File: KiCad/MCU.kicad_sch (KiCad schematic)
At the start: 17 parts, among them U1 RaspberryPi_Pico

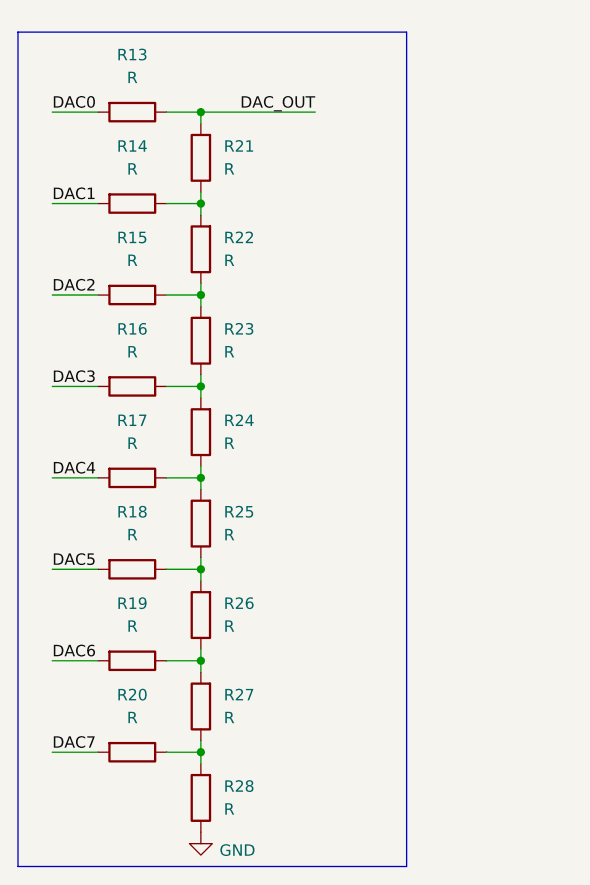
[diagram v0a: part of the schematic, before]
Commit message: Added elements values
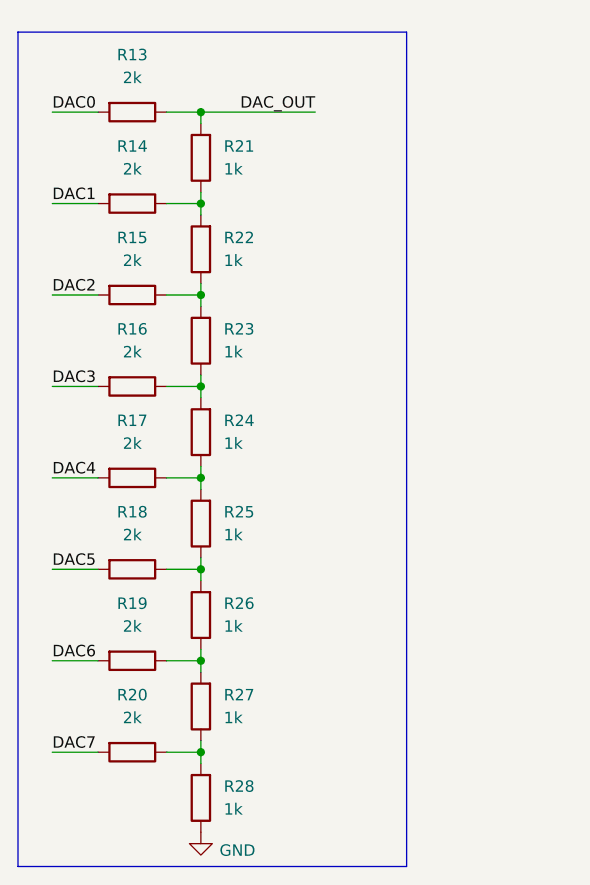
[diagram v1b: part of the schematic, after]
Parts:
- R13, R14, R15, R16, R17, R18, R19, R20: value R -> 2k
- R21, R22, R23, R24, R25, R26, R27, R28: value R -> 1k
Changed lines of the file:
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@@
 			)
 		)
-		(property "Value" "R"
+		(property "Value" "2k"
 			(at 78.74 132.08 90)
 			(effects
@@
 			)
 		)
-		(property "Value" "R"
+		(property "Value" "2k"
 			(at 78.74 71.12 90)
 			(effects
@@
 			)
 		)
-		(property "Value" "R"
+		(property "Value" "1k"
 			(at 88.9 111.7599 0)
 			(effects
@@
 			)
 		)
-		(property "Value" "R"
+		(property "Value" "2k"
 			(at 78.74 81.28 90)
 			(effects
@@
 			)
 		)
-		(property "Value" "R"
+		(property "Value" "2k"
 			(at 78.74 91.44 90)
 			(effects
@@
 			)
 		)
-		(property "Value" "R"
+		(property "Value" "1k"
 			(at 88.9 132.0799 0)
 			(effects
@@
 			)
 		)
-		(property "Value" "R"
+		(property "Value" "2k"
 			(at 78.74 121.92 90)
 			(effects
@@
 			)
 		)
-		(property "Value" "R"
+		(property "Value" "2k"
 			(at 78.74 60.96 90)
 			(effects
@@
 			)
 		)
-		(property "Value" "R"
+		(property "Value" "2k"
 			(at 78.74 111.76 90)
 			(effects
@@
 			)
 		)
-		(property "Value" "R"
+		(property "Value" "2k"
 			(at 78.74 101.6 90)
 			(effects
@@
 			)
 		)
-		(property "Value" "R"
+		(property "Value" "1k"
 			(at 88.9 71.1199 0)
 			(effects
@@
 			)
 		)
-		(property "Value" "R"
+		(property "Value" "1k"
 			(at 88.9 91.4399 0)
 			(effects
@@
 			)
 		)
-		(property "Value" "R"
+		(property "Value" "1k"
 			(at 88.9 101.5999 0)
 			(effects
@@
 			)
 		)
-		(property "Value" "R"
+		(property "Value" "1k"
 			(at 88.9 142.2399 0)
 			(effects
@@
 			)
 		)
-		(property "Value" "R"
+		(property "Value" "1k"
 			(at 88.9 121.9199 0)
 			(effects
@@
 			)
 		)
-		(property "Value" "R"
+		(property "Value" "1k"
 			(at 88.9 81.2799 0)
 			(effects

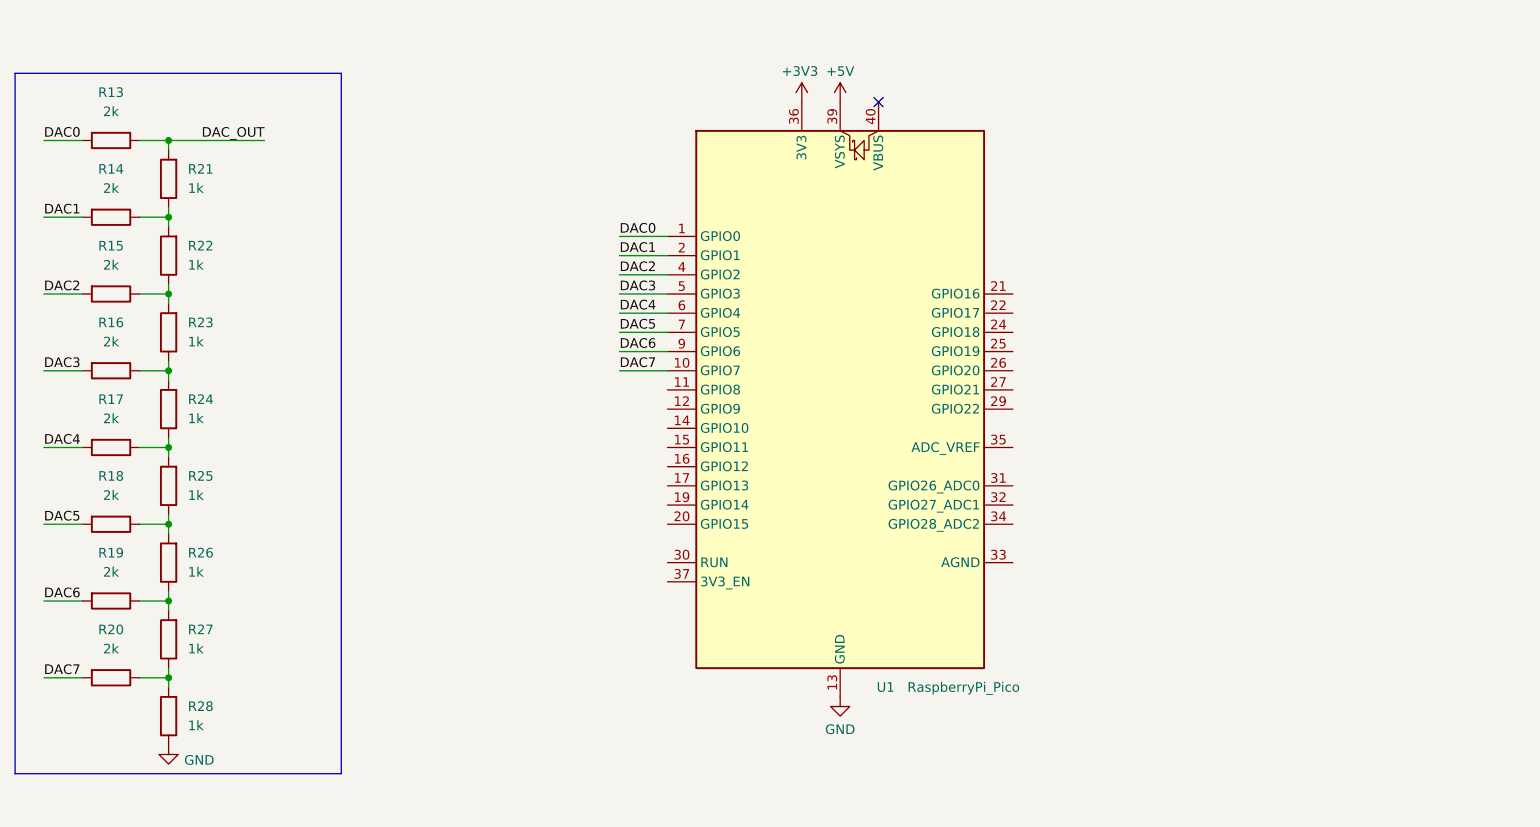
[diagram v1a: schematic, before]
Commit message: Filled in schematic
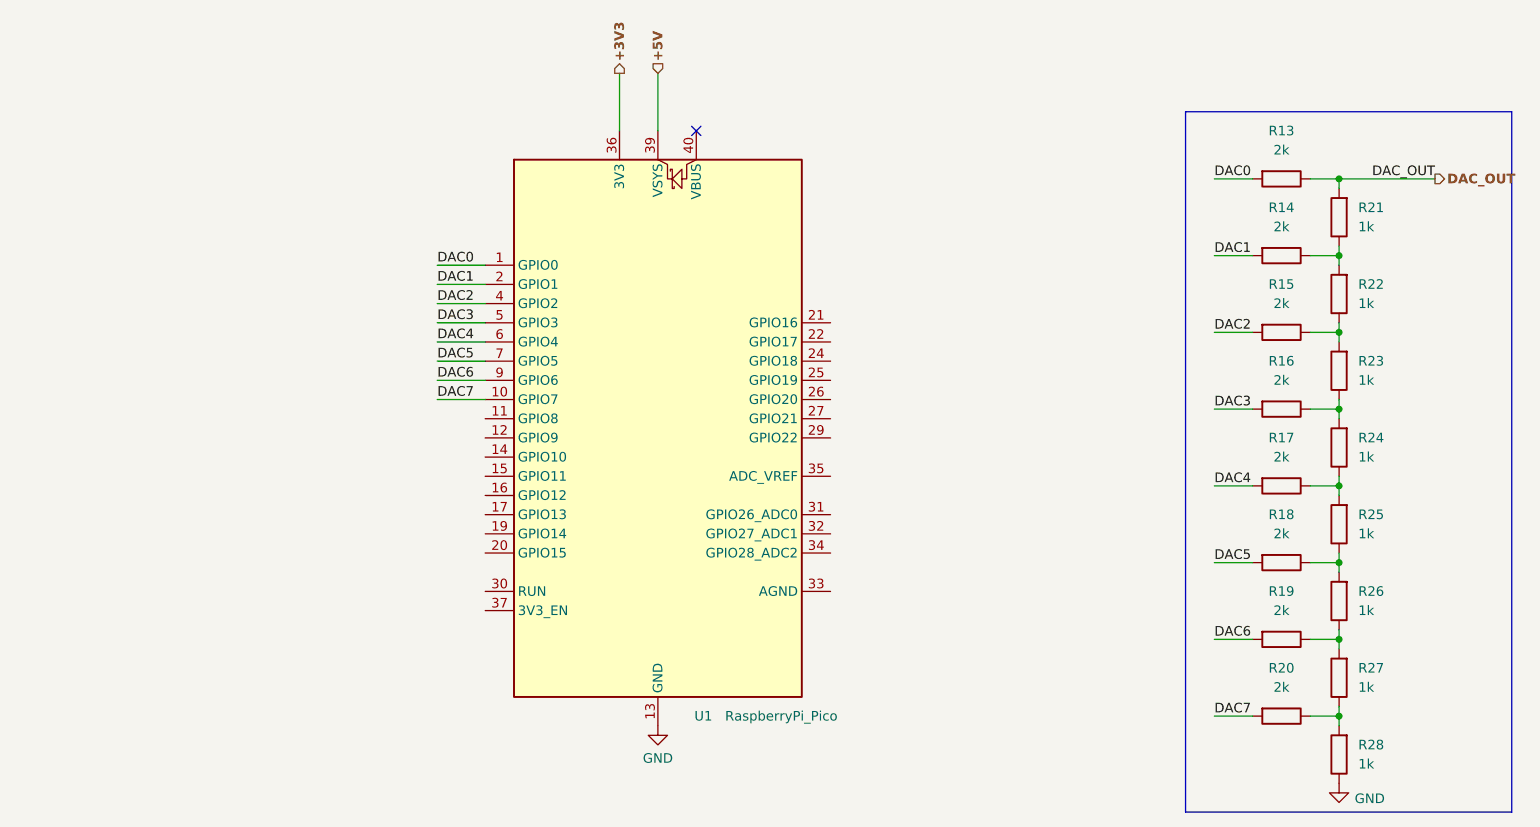
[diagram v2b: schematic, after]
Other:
- moved on the sheet: R13, R14, R15, R16, R17, R18, R19, R20, R21, R22, R23, R24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

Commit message: Added footprints
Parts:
- R13, R14, R15, R16, R17, R18, R19, R20, R21, R22, R23, R24, R25, R26, R27, R28: footprint (none) -> Resistor_SMD:R_0805_2012Metric_Pad1.20x1.40mm_HandSolder
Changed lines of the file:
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@@
 			)
 		)
-		(property "Footprint" ""
+		(property "Footprint" "Resistor_SMD:R_0805_2012Metric_Pad1.20x1.40mm_HandSolder"
 			(at 233.68 139.192 90)
 			(effects
@@
 			)
 		)
-		(property "Footprint" ""
+		(property "Footprint" "Resistor_SMD:R_0805_2012Metric_Pad1.20x1.40mm_HandSolder"
 			(at 233.68 78.232 90)
 			(effects
@@
 			)
 		)
-		(property "Footprint" ""
+		(property "Footprint" "Resistor_SMD:R_0805_2012Metric_Pad1.20x1.40mm_HandSolder"
 			(at 243.078 115.57 90)
 			(effects
@@
 			)
 		)
-		(property "Footprint" ""
+		(property "Footprint" "Resistor_SMD:R_0805_2012Metric_Pad1.20x1.40mm_HandSolder"
 			(at 233.68 88.392 90)
 			(effects
@@
 			)
 		)
-		(property "Footprint" ""
+		(property "Footprint" "Resistor_SMD:R_0805_2012Metric_Pad1.20x1.40mm_HandSolder"
 			(at 233.68 98.552 90)
 			(effects
@@
 			)
 		)
-		(property "Footprint" ""
+		(property "Footprint" "Resistor_SMD:R_0805_2012Metric_Pad1.20x1.40mm_HandSolder"
 			(at 243.078 135.89 90)
 			(effects
@@
 			)
 		)
-		(property "Footprint" ""
+		(property "Footprint" "Resistor_SMD:R_0805_2012Metric_Pad1.20x1.40mm_HandSolder"
 			(at 233.68 129.032 90)
 			(effects
@@
 			)
 		)
-		(property "Footprint" ""
+		(property "Footprint" "Resistor_SMD:R_0805_2012Metric_Pad1.20x1.40mm_HandSolder"
 			(at 233.68 68.072 90)
 			(effects
@@
 			)
 		)
-		(property "Footprint" ""
+		(property "Footprint" "Resistor_SMD:R_0805_2012Metric_Pad1.20x1.40mm_HandSolder"
 			(at 233.68 118.872 90)
 			(effects
@@
 			)
 		)
-		(property "Footprint" ""
+		(property "Footprint" "Resistor_SMD:R_0805_2012Metric_Pad1.20x1.40mm_HandSolder"
 			(at 233.68 108.712 90)
 			(effects
@@
 			)
 		)
-		(property "Footprint" ""
+		(property "Footprint" "Resistor_SMD:R_0805_2012Metric_Pad1.20x1.40mm_HandSolder"
 			(at 243.078 74.93 90)
 			(effects
@@
 			)
 		)
-		(property "Footprint" ""
+		(property "Footprint" "Resistor_SMD:R_0805_2012Metric_Pad1.20x1.40mm_HandSolder"
 			(at 243.078 95.25 90)
 			(effects
@@
 			)
 		)
-		(property "Footprint" ""
+		(property "Footprint" "Resistor_SMD:R_0805_2012Metric_Pad1.20x1.40mm_HandSolder"
 			(at 243.078 105.41 90)
 			(effects
@@
 			)
 		)
-		(property "Footprint" ""
+		(property "Footprint" "Resistor_SMD:R_0805_2012Metric_Pad1.20x1.40mm_HandSolder"
 			(at 243.078 146.05 90)
 			(effects
@@
 			)
 		)
-		(property "Footprint" ""
+		(property "Footprint" "Resistor_SMD:R_0805_2012Metric_Pad1.20x1.40mm_HandSolder"
 			(at 243.078 125.73 90)
 			(effects
@@
 			)
 		)
-		(property "Footprint" ""
+		(property "Footprint" "Resistor_SMD:R_0805_2012Metric_Pad1.20x1.40mm_HandSolder"
 			(at 243.078 85.09 90)
 			(effects
